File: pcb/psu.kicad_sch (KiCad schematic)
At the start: 17 parts, among them J1 USB4105-GF-A, U3 MCP73831/OT, U4 AP2112K-3.3, U5 450405020524

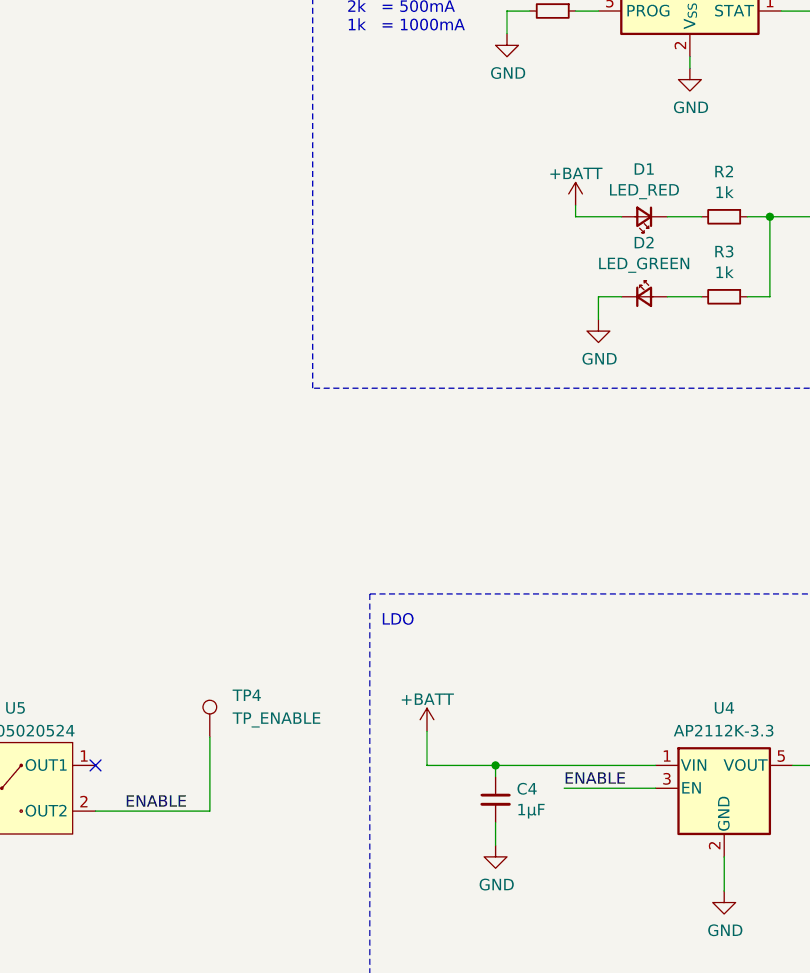
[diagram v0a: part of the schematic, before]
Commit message: Replaces nRF52840 with ESP32-S3
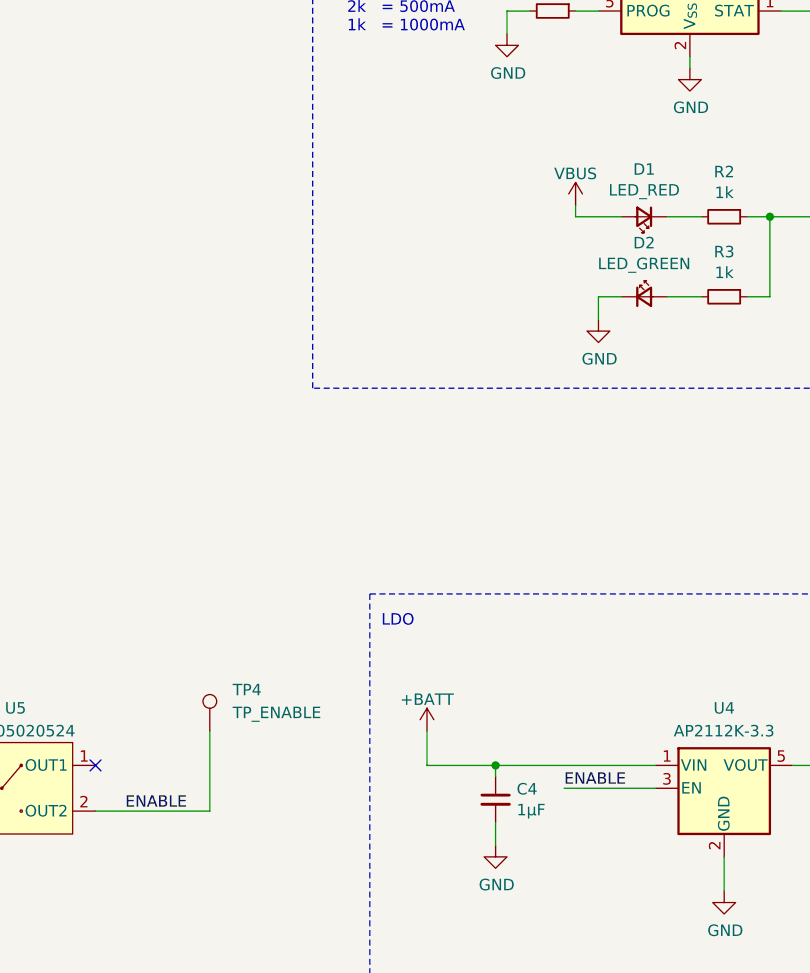
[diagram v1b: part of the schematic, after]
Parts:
- TP4: footprint TestPoint:TestPoint_Pad_D2.0mm -> TestPoint:TestPoint_Pad_D1.5mm
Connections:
- net +BATT: no longer D1.2 (A)
- net VBUS: now also D1.2 (A)
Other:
- moved on the sheet: TP4
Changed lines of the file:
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@@
     (stroke (width 0) (type default))
   )
-  (wire (pts (xy 58.42 146.685) (xy 58.42 154.94))
+  (wire (pts (xy 58.42 146.05) (xy 58.42 154.94))
     (stroke (width 0) (type default))
   )
@@
   (hierarchical_label "USB_D-" (shape input) (at 25.4 21.59 180) (fields_autoplaced)
     (effects (font (size 1.27 1.27)) (justify right))
+  )
+  (symbol (lib_id "power:VBUS") (at 99.06 87.63 0) (unit 1)
+    (in_bom yes) (on_board yes) (dnp no) (fields_autoplaced)
+    (property "Reference" "#PWR01" (at 99.06 91.44 0)
+      (effects (font (size 1.27 1.27)) hide)
+    )
+    (property "Value" "VBUS" (at 99.06 84.1281 0)
+      (effects (font (size 1.27 1.27)))
+    )
+    (property "Footprint" "" (at 99.06 87.63 0)
+      (effects (font (size 1.27 1.27)) hide)
+    )
+    (property "Datasheet" "" (at 99.06 87.63 0)
+      (effects (font (size 1.27 1.27)) hide)
+    )
+    (pin "1")
+    (instances
+      (project "ot-riwa"
+        (path "/27c79cfd-7e0d-4d78-9eed-2a8b043fdd67/56041fc6-6e17-4b0b-abcc-5d5fefb6b277"
+          (reference "#PWR01") (unit 1)
+        )
+        (path "/27c79cfd-7e0d-4d78-9eed-2a8b043fdd67/56041fc6-6e17-4b0b-abcc-5d5fefb6b277/76cd64a2-82d5-44eb-8e66-b56b87ea476d"
+          (reference "#PWR03") (unit 1)
+        )
+      )
+      (project "rep-trap-pcb"
+        (path "/b363dc8f-4a45-4779-a397-ccb82393dab8/eebb1d37-a01d-4adf-be70-a8e8f9293475/23008b32-6835-495f-a93f-d60d3125c4cb"
+          (reference "#PWR014") (unit 1)
+        )
+      )
+    )
   )
   (symbol (lib_id "450405020524:450405020524") (at 36.83 152.4 0) (unit 1)
@@
     )
   )
-  (symbol (lib_id "Connector:TestPoint") (at 58.42 146.685 0) (unit 1)
+  (symbol (lib_id "Connector:TestPoint") (at 58.42 146.05 0) (unit 1)
     (in_bom no) (on_board yes) (dnp no) (fields_autoplaced)
-    (property "Reference" "TP4" (at 60.96 142.113 0)
+    (property "Reference" "TP4" (at 60.96 141.478 0)
       (effects (font (size 1.27 1.27)) (justify left))
     )
-    (property "Value" "TP_ENABLE" (at 60.96 144.653 0)
+    (property "Value" "TP_ENABLE" (at 60.96 144.018 0)
       (effects (font (size 1.27 1.27)) (justify left))
     )
-    (property "Footprint" "TestPoint:TestPoint_Pad_D2.0mm" (at 63.5 146.685 0)
-      (effects (font (size 1.27 1.27)) hide)
-    )
-    (property "Datasheet" "~" (at 63.5 146.685 0)
+    (property "Footprint" "TestPoint:TestPoint_Pad_D1.5mm" (at 63.5 146.05 0)
+      (effects (font (size 1.27 1.27)) hide)
+    )
+    (property "Datasheet" "~" (at 63.5 146.05 0)
       (effects (font (size 1.27 1.27)) hide)
     )
@@
         )
       )
-    )
-  )
-  (symbol (lib_id "power:+BATT") (at 99.06 87.63 0) (unit 1)
-    (in_bom yes) (on_board yes) (dnp no) (fields_autoplaced)
-    (property "Reference" "#PWR05" (at 99.06 91.44 0)
-      (effects (font (size 1.27 1.27)) hide)
-    )
-    (property "Value" "+BATT" (at 99.06 84.1281 0)
-      (effects (font (size 1.27 1.27)))
-    )
-    (property "Footprint" "" (at 99.06 87.63 0)
-      (effects (font (size 1.27 1.27)) hide)
-    )
-    (property "Datasheet" "" (at 99.06 87.63 0)
-      (effects (font (size 1.27 1.27)) hide)
-    )
-    (pin "1")
-    (instances
-      (project "ot-riwa"
-        (path "/27c79cfd-7e0d-4d78-9eed-2a8b043fdd67/56041fc6-6e17-4b0b-abcc-5d5fefb6b277"
-          (reference "#PWR05") (unit 1)
-        )
-        (path "/27c79cfd-7e0d-4d78-9eed-2a8b043fdd67/56041fc6-6e17-4b0b-abcc-5d5fefb6b277/76cd64a2-82d5-44eb-8e66-b56b87ea476d"
-          (reference "#PWR03") (unit 1)
-        )
-      )
-      (project "rep-trap-pcb"
-        (path "/b363dc8f-4a45-4779-a397-ccb82393dab8/eebb1d37-a01d-4adf-be70-a8e8f9293475/23008b32-6835-495f-a93f-d60d3125c4cb"
-          (reference "#PWR020") (unit 1)
-        )
-      )

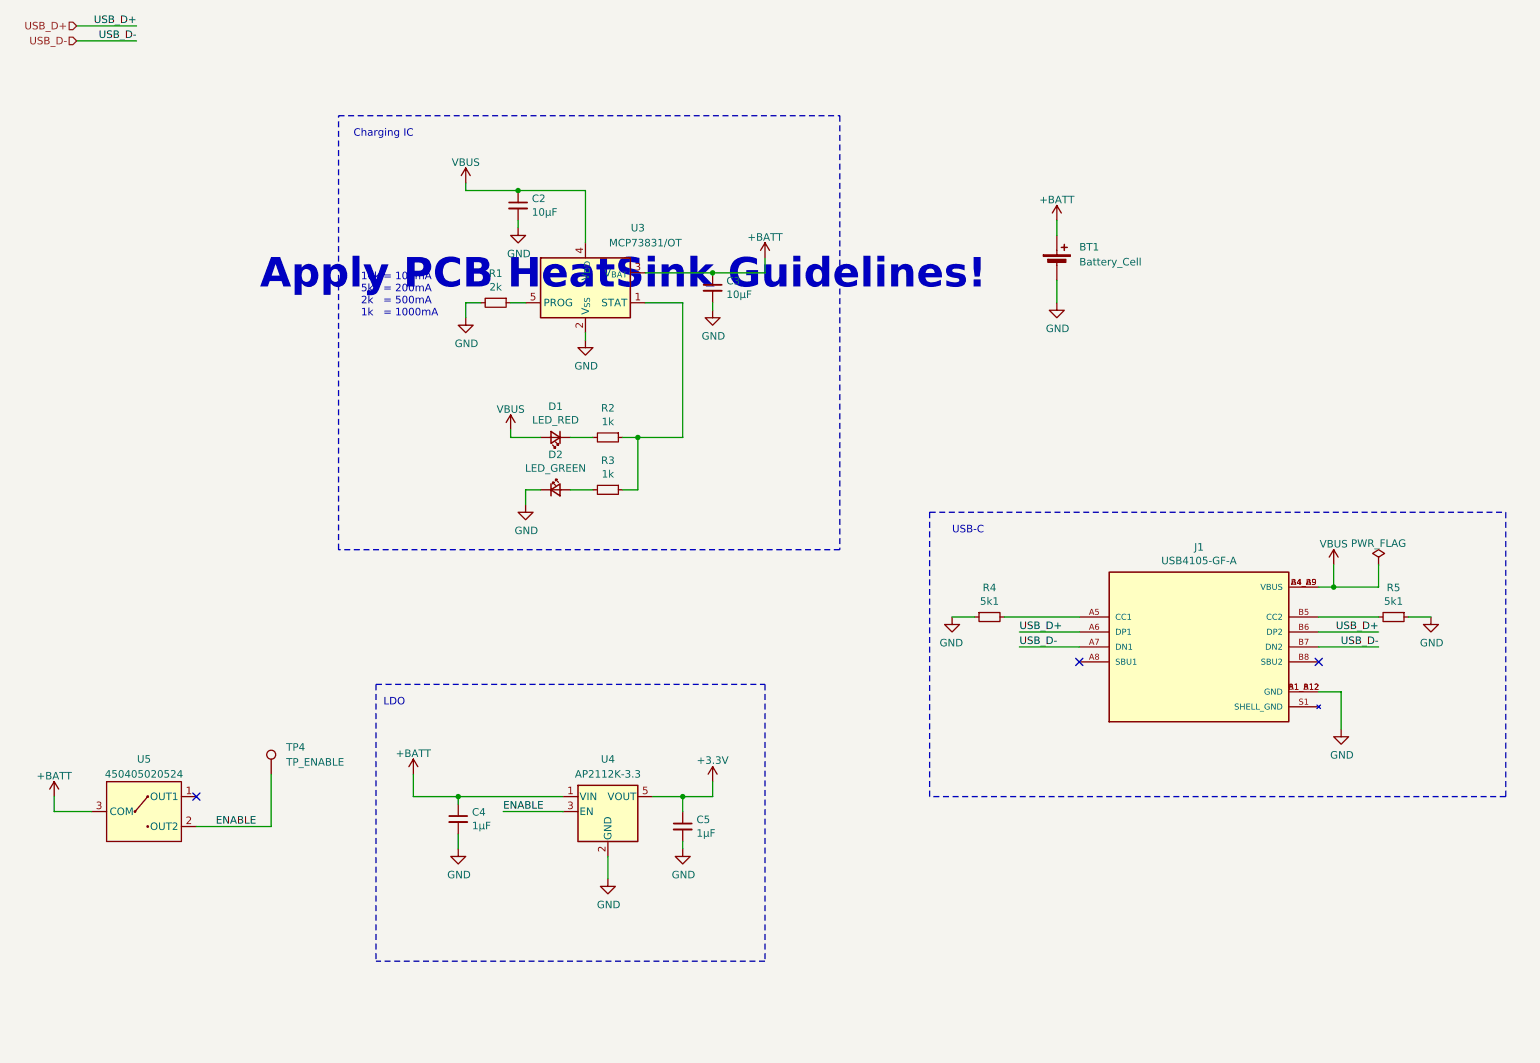
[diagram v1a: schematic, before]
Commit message: Layout all components
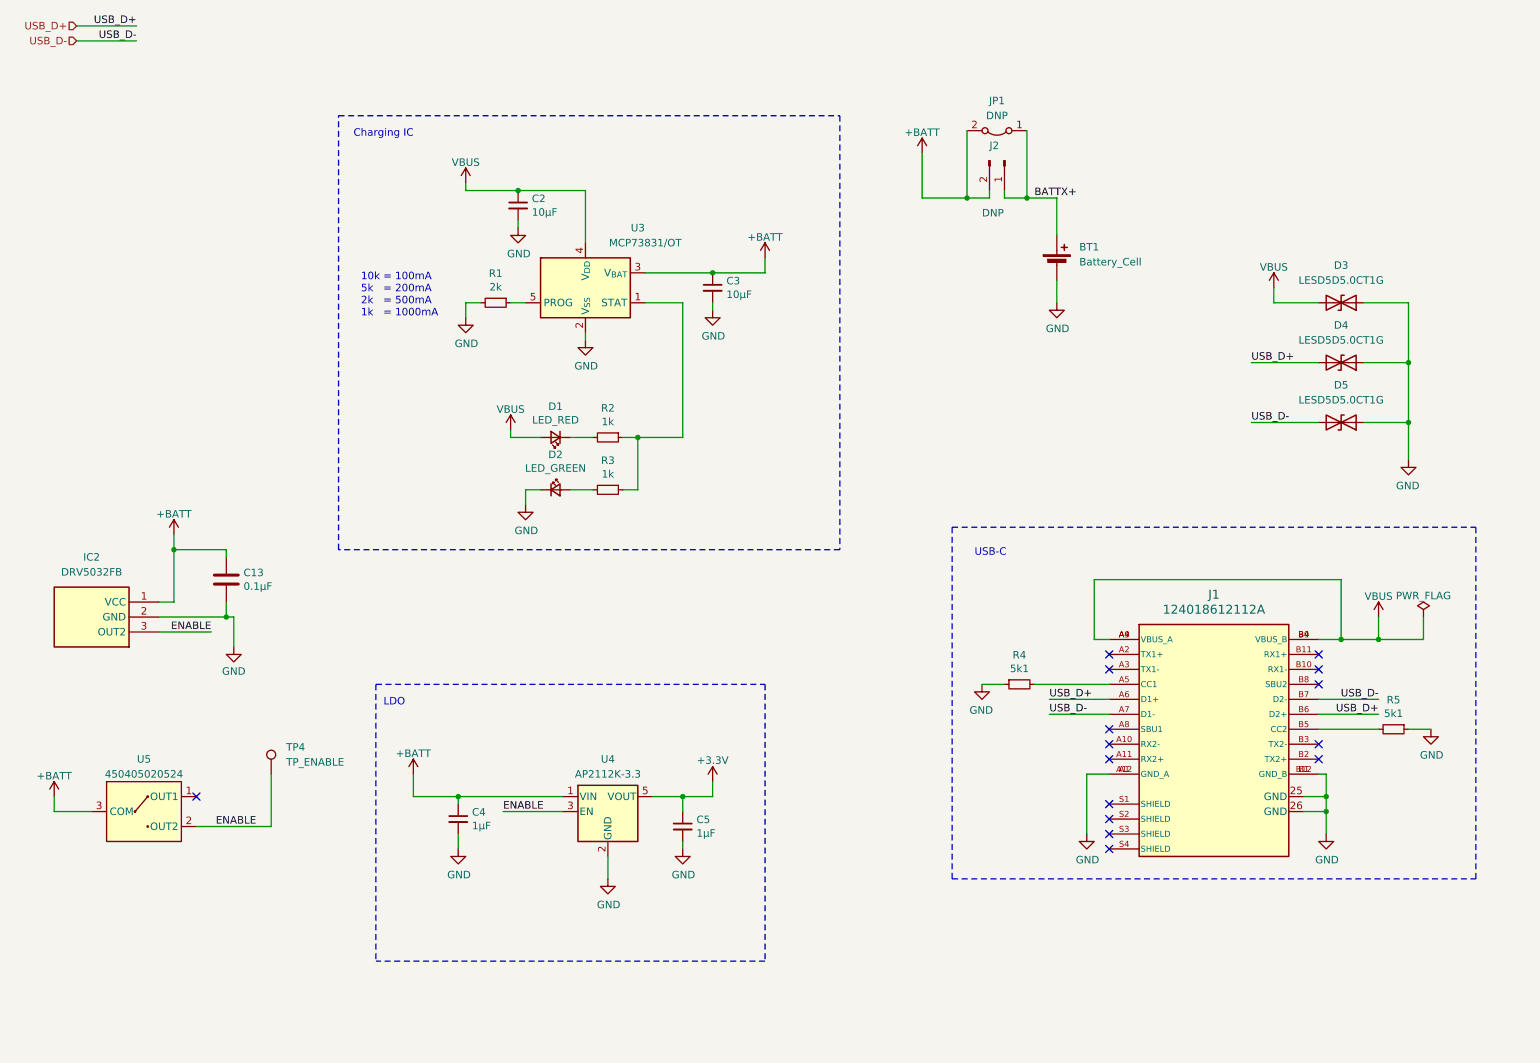
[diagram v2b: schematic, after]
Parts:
- removed J1: USB4105-GF-A, USB4105-GF-A:GCT_USB4105-GF-A, symbol USB4105-GF-A:USB4105-GF-A
- added C13: 0.1µF, Capacitor_SMD:C_0603_1608Metric, symbol Device:C
- added D3, D4, D5: LESD5D5.0CT1G, LESD5D5.0CT1G:LESD5D50CT1G, symbol Device:D_TVS
- added IC2: DRV5032FB, DRV5032DULPGM:DRV5032DULPGM, symbol DRV5032DULPGM:DRV5032DULPGM
- added J1: 124018612112A, 124018612112A:CONN_124018612112A_AMP, symbol 124018612112A:124018612112A
- added J2: DNP, Connector_PinSocket_2.54mm:PinSocket_1x02_P2.54mm_Vertical, symbol Connector:Conn_01x02_Pin
- added JP1: DNP, Jumper:SolderJumper-2_P1.3mm_Bridged_RoundedPad1.0x1.5mm, symbol Jumper:Jumper_2_Bridged
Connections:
- net +BATT: now also C13.1, IC2.1 (VCC), J2.2 (Pin_2), JP1.2 (B); no longer BT1.1 (+)
- net ENABLE: now also IC2.3 (OUT2)
- net GND: now also C13.2, D3.1 (A1), D4.1 (A1), D5.1 (A1), IC2.2 (GND), J1.25 (GND), J1.26 (GND), J1.A1 (GND_A), J1.A12 (GND_A), J1.B1 (GND_B), J1.B12 (GND_B)
- net USB_D+: now also D4.2 (A2), J1.A6 (D1+), J1.B6 (D2+)
- net USB_D-: now also D5.2 (A2), J1.A7 (D1-), J1.B7 (D2-)
- net VBUS: now also D3.2 (A2), J1.A4 (VBUS_A), J1.A9 (VBUS_A), J1.B4 (VBUS_B), J1.B9 (VBUS_B)
- net at R4.2: now also J1.A5 (CC1)
- net at R5.2: now also J1.B5 (CC2)
- new net BATTX+: BT1.1 (+), J2.1 (Pin_1), JP1.1 (A)
- no-connect marks 3 -> 15
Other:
- note removed: "Apply PCB HeatSink Guidelines!"
- moved on the sheet: R4, R5

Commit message: Refactored layout + silkscreen + added I2C connector
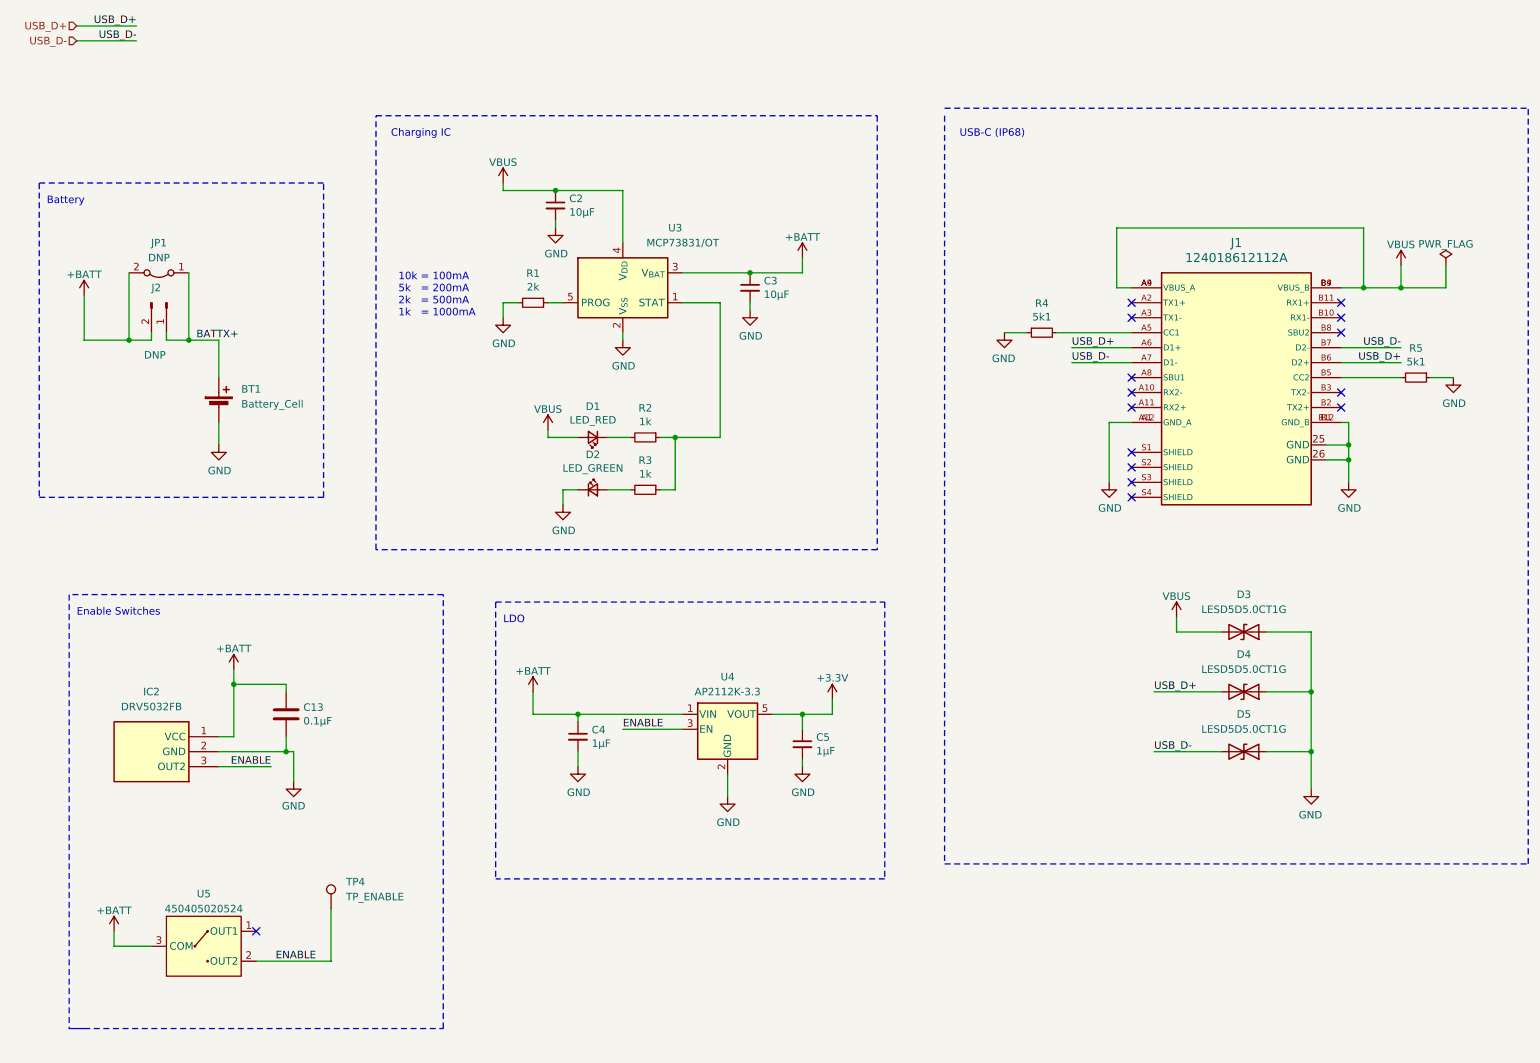
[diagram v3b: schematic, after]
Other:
- note added: "Battery"
- note added: "Enable Switches"
- note added: "USB-C (IP68)"
- note removed: "USB-C"
- moved on the sheet: BT1, C13, C2, C3, C4, C5, D1, D2, D3, D4, D5, IC2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

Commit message: Refactored components
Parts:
- C13: value 0.1µF -> 0.1uF
- C2, C3: value 10µF -> 10uF
- C4, C5: value 1µF -> 1uF
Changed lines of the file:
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@@
       (effects (font (size 1.27 1.27)) (justify left))
     )
-    (property "Value" "10µF" (at 109.0168 50.673 0)
+    (property "Value" "10uF" (at 109.0168 50.673 0)
       (effects (font (size 1.27 1.27)) (justify left))
     )
@@
       (effects (font (size 1.27 1.27)) (justify left))
     )
-    (property "Value" "0.1µF" (at 63.881 137.033 0)
+    (property "Value" "0.1uF" (at 63.881 137.033 0)
       (effects (font (size 1.27 1.27)) (justify left))
     )
@@
       (effects (font (size 1.27 1.27)) (justify left))
     )
-    (property "Value" "1µF" (at 150.9268 142.113 0)
+    (property "Value" "1uF" (at 150.9268 142.113 0)
       (effects (font (size 1.27 1.27)) (justify left))
     )
@@
       (effects (font (size 1.27 1.27)) (justify left))
     )
-    (property "Value" "1µF" (at 112.8268 140.843 0)
+    (property "Value" "1uF" (at 112.8268 140.843 0)
       (effects (font (size 1.27 1.27)) (justify left))
     )
@@
       (effects (font (size 1.27 1.27)) (justify left))
     )
-    (property "Value" "10µF" (at 142.0368 64.643 0)
-      (effects (font (size 1.27 1.27)) (justify left))
-    )
+    (property "Value" "10uF" (at 142.0368 64.643 0)
+      (effects (font (size 1.27 1.27)) (justify left))
+    )

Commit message: Implement RTC and device sync + updated 3d objects
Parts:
- added R13: 4.7k, Resistor_SMD:R_0603_1608Metric, symbol Device:R_Small
- added R14: 10k, Resistor_SMD:R_0603_1608Metric, symbol Device:R_Small
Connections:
- net GND: now also R14.2
- net VBUS: now also R13.1
- new net VBUS_DETECT: R13.2, R14.1
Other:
- note added: "USB DETECT"
- moved on the sheet: C2, C3, C4, C5, D1, D2, R1, R2, R3, U3, U4
